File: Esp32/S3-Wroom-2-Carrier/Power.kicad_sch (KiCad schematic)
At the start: 11 parts, among them J3 USB_C_Receptacle_USB2.0_16P, U2 ADM7171ACPZ-3.0-R7

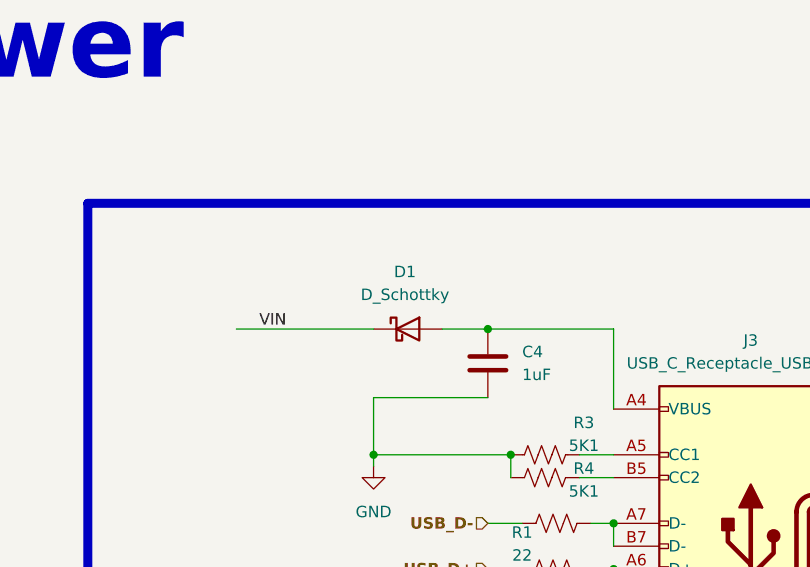
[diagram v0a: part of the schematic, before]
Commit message: Connectors
Lower connector routed
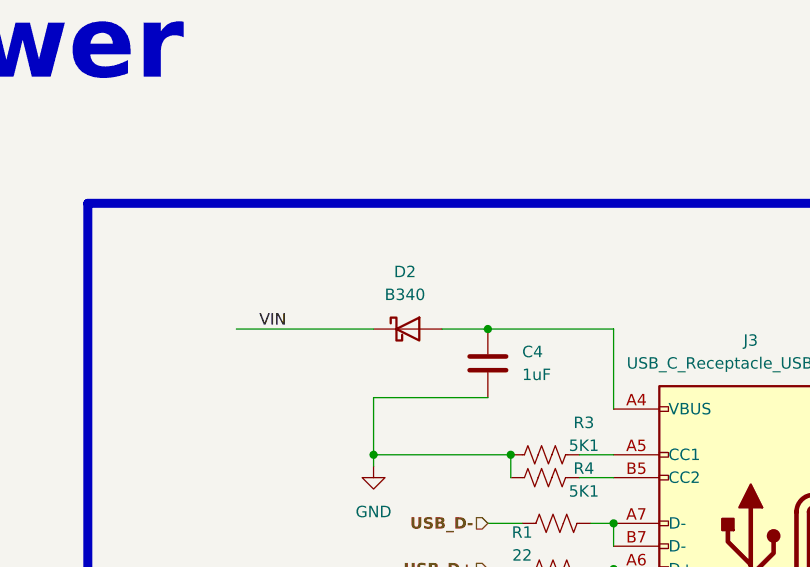
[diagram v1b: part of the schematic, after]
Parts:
- removed D1: D_Schottky, symbol Device:D_Schottky
- added D2: B340, Diode_SMD:D_SMA, symbol Diode:B340
- J3: footprint (none) -> Connector_USB:USB_C_Receptacle_Palconn_UTC16-G
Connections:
- net VIN: now also D2.1 (K)
- net at C4.1, J3.A4 (VBUS), J3.A9 (VBUS)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: now also D2.2 (A)
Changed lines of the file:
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@@
+	)
+	(symbol
+		(lib_id "Diode:B340")
+		(at 203.2 59.69 0)
+		(unit 1)
+		(exclude_from_sim no)
+		(in_bom yes)
+		(on_board yes)
+		(dnp no)
+		(fields_autoplaced yes)
+		(property "Reference" "D2"
+			(at 202.8825 53.34 0)
+			(effects
+				(font
+					(size 1.27 1.27)
+				)
+			)
+		)
+		(property "Value" "B340"
+			(at 202.8825 55.88 0)
+			(effects
+				(font
+					(size 1.27 1.27)
+				)
+			)
+		)
+		(property "Footprint" "Diode_SMD:D_SMA"
+			(at 203.2 64.135 0)
+			(effects
+				(font
+					(size 1.27 1.27)
+				)
+				(hide yes)
+			)
+		)
+		(property "Datasheet" "http://www.jameco.com/Jameco/Products/ProdDS/1538777.pdf"
+			(at 203.2 59.69 0)
+			(effects
+				(font
+					(size 1.27 1.27)
+				)
+				(hide yes)
+			)
+		)
+		(property "Description" "40V 3A Schottky Barrier Rectifier Diode, SMC"
+			(at 203.2 59.69 0)
+			(effects
+				(font
+					(size 1.27 1.27)
+				)
+				(hide yes)
+			)
+		)
+		(pin "2"
+		)
+		(pin "1"
+		)
+		(instances
+			(project ""
+				(path "/0650c7a8-acba-429c-9f8e-eec0baf0bc1c/fede4c36-00cc-4d3d-b71c-5243ba232202/1ed0de36-db97-4a97-8558-e1b0192db54f"
+					(reference "D2")
+					(unit 1)
+				)
+			)
+		)
 	)
 	(symbol
@@
 			)
 		)
-		(property "Footprint" ""
+		(property "Footprint" "Connector_USB:USB_C_Receptacle_Palconn_UTC16-G"
 			(at 237.49 83.82 0)
 			(effects
@@
 					(unit 1)
 				)
-			)
-		)
-	)
-	(symbol
-		(lib_id "Device:D_Schottky")
-		(at 203.2 59.69 0)
-		(unit 1)
-		(exclude_from_sim no)
-		(in_bom yes)
-		(on_board yes)
-		(dnp no)
-		(fields_autoplaced yes)
-		(property "Reference" "D1"
-			(at 202.8825 53.34 0)
-			(effects
-				(font
-					(size 1.27 1.27)
-				)
-			)
-		)
-		(property "Value" "D_Schottky"
-			(at 202.8825 55.88 0)
-			(effects
-				(font
-					(size 1.27 1.27)
-				)
-			)
-		)
-		(property "Footprint" ""
-			(at 203.2 59.69 0)
-			(effects
-				(font
-					(size 1.27 1.27)
-				)
-				(hide yes)
-			)
-		)
-		(property "Datasheet" "~"
-			(at 203.2 59.69 0)
-			(effects
-				(font
-					(size 1.27 1.27)
-				)
-				(hide yes)
-			)
-		)
-		(property "Description" "Schottky diode"
-			(at 203.2 59.69 0)
-			(effects
-				(font
-					(size 1.27 1.27)
-				)
-				(hide yes)
-			)
-		)
-		(pin "2"
-		)
-		(pin "1"
-		)
-		(instances
-			(project ""
-				(path "/0650c7a8-acba-429c-9f8e-eec0baf0bc1c/fede4c36-00cc-4d3d-b71c-5243ba232202/1ed0de36-db97-4a97-8558-e1b0192db54f"
-					(reference "D1")
-					(unit 1)
-				)

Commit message: Routing
Routing finished needs to be verify
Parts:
- removed J3: USB_C_Receptacle_USB2.0_16P, Connector_USB:USB_C_Receptacle_Palconn_UTC16-G, symbol Connector:USB_C_Receptacle_USB2.0_16P
- removed R3, R4: 5K1, Resistor_SMD:R_0805_2012Metric_Pad1.20x1.40mm_HandSolder, symbol Device:R_US
- added D1, D3: ~, User_Footprint:DIOC1608X36N, symbol _Misc_Symbols:PGB1010603NR
- added J2: 65100516121, User_Footprint:Usb_B_mini_Wurth_65100516121, symbol _Connectors:Usb_Mini_B_65100516121
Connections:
- net GND: now also D1.1, D3.1, J2.5 (GND), J2.S1, J2.S2, J2.S3, J2.S4
- net at R2.2: now also D1.2, J2.3 (D+)
- net at R1.2: now also D3.2, J2.2 (D-)
- net VBUS: now reaches C4.1, D2.2 (A)
- net VBUS: now also J2.1 (VBUS)
- no-connect marks 2 -> 1
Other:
- moved on the sheet: R1, R2

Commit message: Connectors
change one connector from 21 to 25 pins
Added test points
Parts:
- added R3: 100K, Resistor_SMD:R_0805_2012Metric_Pad1.20x1.40mm_HandSolder, symbol Device:R_US
- added TP1: 3V3, TestPoint:TestPoint_Pad_1.0x1.0mm, symbol Connector:TestPoint
- added TP2: VIN, TestPoint:TestPoint_Pad_1.0x1.0mm, symbol Connector:TestPoint
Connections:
- net +3V3: now also R3.2, TP1.1
- net VIN: now also TP2.1
- net EN renamed PWR_EN
- net PWR_EN: now also R3.1
